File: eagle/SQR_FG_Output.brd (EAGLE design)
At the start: 42.9 x 30.5 mm, 17 parts, among them IC2 NJM7032, T1 2SK4017, T2 2SK4017

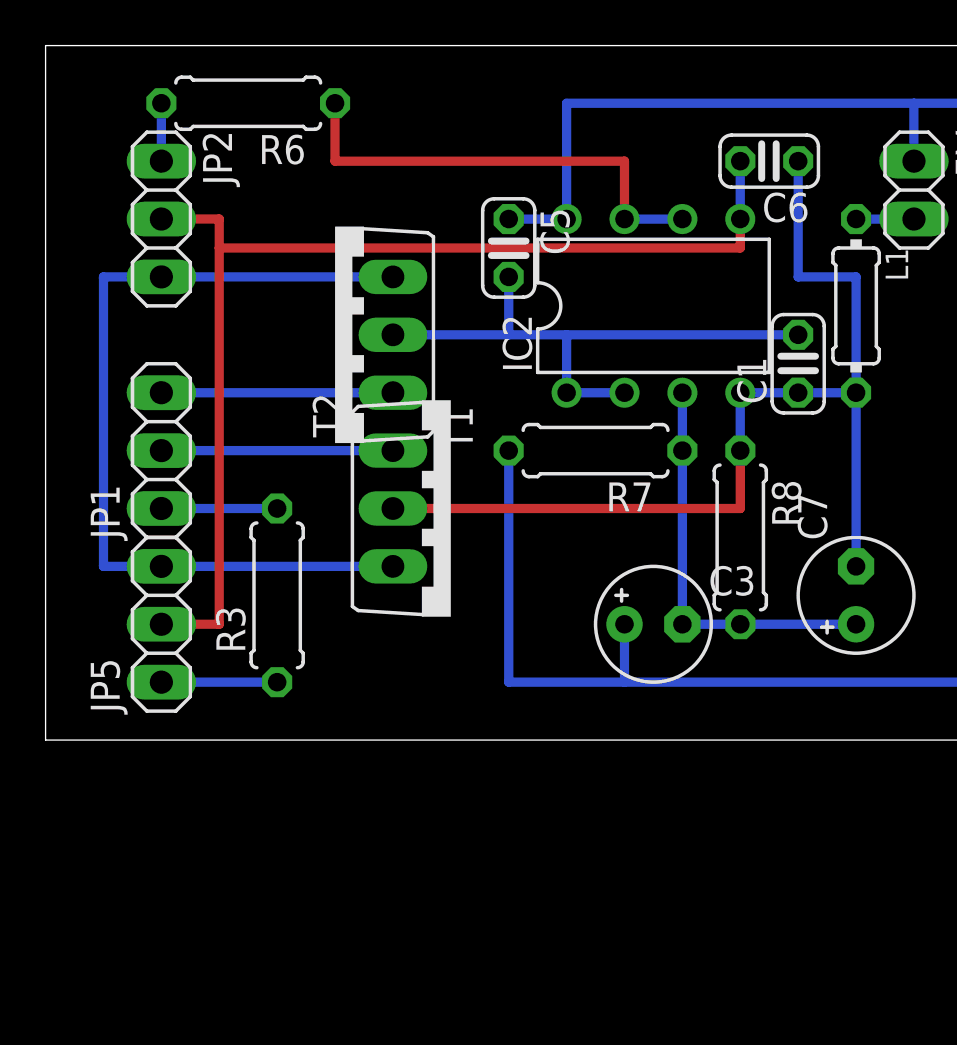
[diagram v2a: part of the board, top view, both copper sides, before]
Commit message: SQR_FG_Output.sch LC 2次LPFを追加
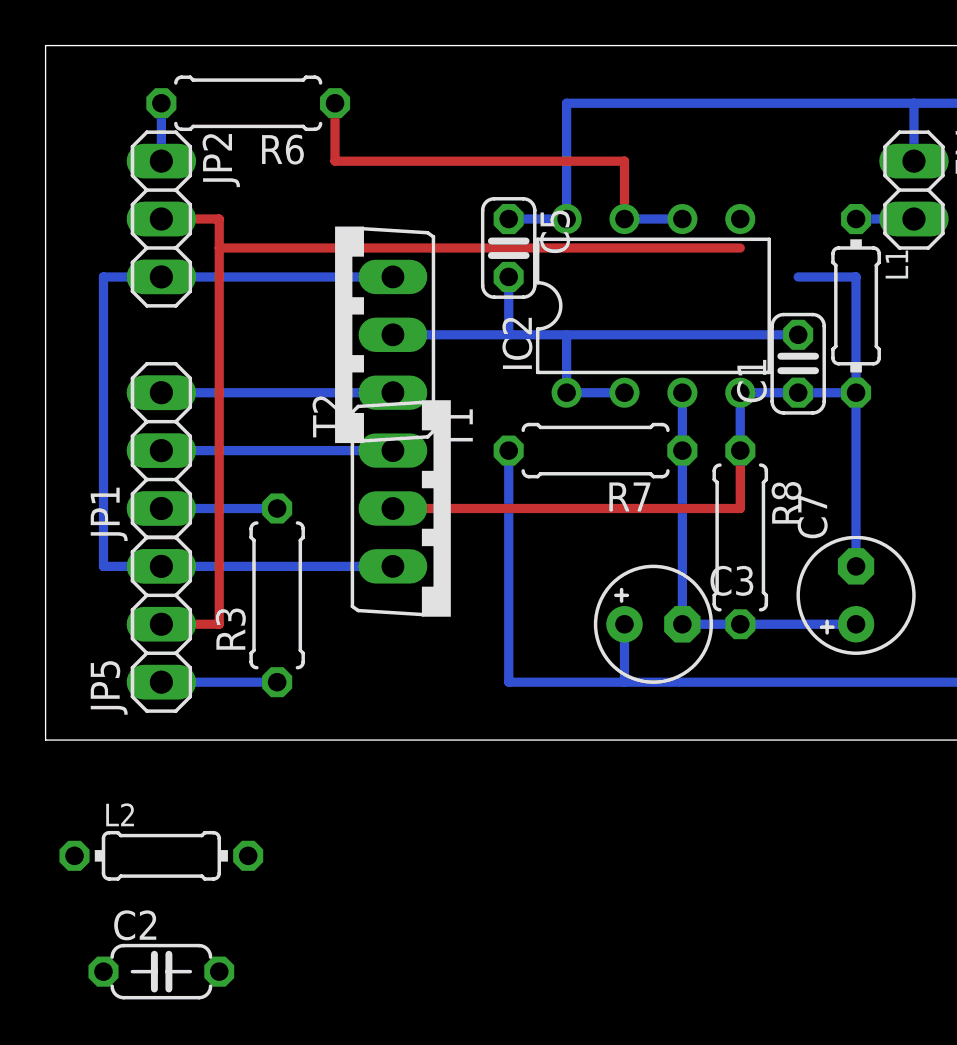
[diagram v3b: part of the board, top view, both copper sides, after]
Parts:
- removed C6: 22pF, rcl:C025-024X044
- added C2: 100p, rcl:C050-024X044
- added L2: 1uH, rcl:0204/7
- R3: value 10k -> 1k
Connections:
- new net N$1: C2.1, IC2.5, L2.2
- net AGND: no longer C6.1
- net BYPASS: now also C2.2, L2.1; no longer C6.2, IC2.5
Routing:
- net AGND: track 45.7 -> 40.6 mm
- net BYPASS: track 49.5 -> 45.7 mm
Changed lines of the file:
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@@
 <element name="C3" library="rcl" package="E2,5-5" value="100uF" x="26.67" y="5.08"/>
 <element name="C5" library="rcl" package="C025-024X044" value="0.1uF" x="20.32" y="21.59" rot="R270"/>
-<element name="C6" library="rcl" package="C025-024X044" value="22pF" x="31.75" y="25.4" rot="R180"/>
 <element name="C7" library="rcl" package="E2,5-5" value="100uF" x="35.56" y="6.35" rot="R90"/>
 <element name="IC2" library="linear" package="DIL08" value="NJM7032" x="26.67" y="19.05"/>
 <element name="JP5" library="pinhead" package="1X03" value="Level" x="5.08" y="5.08" rot="R90"/>
-<element name="R3" library="rcl" package="0207/7" value="10k" x="10.16" y="6.35" rot="R90"/>
+<element name="R3" library="rcl" package="0207/7" value="1k" x="10.16" y="6.35" rot="R90"/>
 <element name="R6" library="rcl" package="0207/7" value="10" x="8.89" y="27.94" rot="R180"/>
 <element name="R7" library="rcl" package="0207/7" value="10k" x="24.13" y="12.7" rot="R180"/>
@@
 <element name="L1" library="rcl" package="0204/7" value="1uH" x="35.56" y="19.05" rot="R270"/>
 <element name="JP2" library="pinhead" package="1X03" value="" x="5.08" y="22.86" rot="R270"/>
+<element name="L2" library="rcl" package="0204/7" value="1uH" x="5.08" y="-5.08"/>
+<element name="C2" library="rcl" package="C050-024X044" value="100p" x="5.08" y="-10.16"/>
 </elements>
 <signals>
@@
 </signal>
 <signal name="BYPASS">
-<contactref element="C6" pad="2"/>
 <contactref element="JP5" pad="2"/>
-<contactref element="IC2" pad="5"/>
-<wire x1="30.48" y1="25.4" x2="30.48" y2="22.86" width="0.4064" layer="16"/>
-<wire x1="30.48" y1="22.86" x2="30.48" y2="21.59" width="0.4064" layer="1"/>
 <wire x1="30.48" y1="21.59" x2="7.62" y2="21.59" width="0.4064" layer="1"/>
 <wire x1="7.62" y1="21.59" x2="7.62" y2="5.08" width="0.4064" layer="1"/>
@@
 <wire x1="5.08" y1="22.86" x2="7.62" y2="22.86" width="0.4064" layer="1"/>
 <wire x1="7.62" y1="22.86" x2="7.62" y2="21.59" width="0.4064" layer="1"/>
+<contactref element="L2" pad="1"/>
+<contactref element="C2" pad="2"/>
+<wire x1="1.27" y1="-5.08" x2="5.08" y2="5.08" width="0" layer="19" extent="1-1"/>
+<wire x1="7.62" y1="-10.16" x2="1.27" y2="-5.08" width="0" layer="19" extent="1-1"/>
 </signal>
 <signal name="AGND">
 <contactref element="T2" pad="2"/>
-<contactref element="C6" pad="1"/>
 <contactref element="R8" pad="1"/>
 <contactref element="C7" pad="-"/>
@@
 <wire x1="35.56" y1="15.24" x2="35.56" y2="20.32" width="0.4064" layer="16"/>
 <wire x1="35.56" y1="20.32" x2="33.02" y2="20.32" width="0.4064" layer="16"/>
-<wire x1="33.02" y1="20.32" x2="33.02" y2="25.4" width="0.4064" layer="16"/>
 <wire x1="35.56" y1="7.62" x2="35.56" y2="15.24" width="0.4064" layer="16"/>
 <wire x1="15.24" y1="10.16" x2="30.48" y2="10.16" width="0.4064" layer="1"/>
@@
 <wire x1="35.56" y1="22.86" x2="38.1" y2="22.86" width="0.4064" layer="16"/>
 </signal>
+<signal name="N$1">
+<contactref element="L2" pad="2"/>
+<contactref element="IC2" pad="5"/>
+<contactref element="C2" pad="1"/>
+<wire x1="8.89" y1="-5.08" x2="30.48" y2="22.86" width="0" layer="19" extent="1-1"/>
+<wire x1="2.54" y1="-10.16" x2="8.89" y2="-5.08" width="0" layer="19" extent="1-1"/>
+</signal>
 </signals>

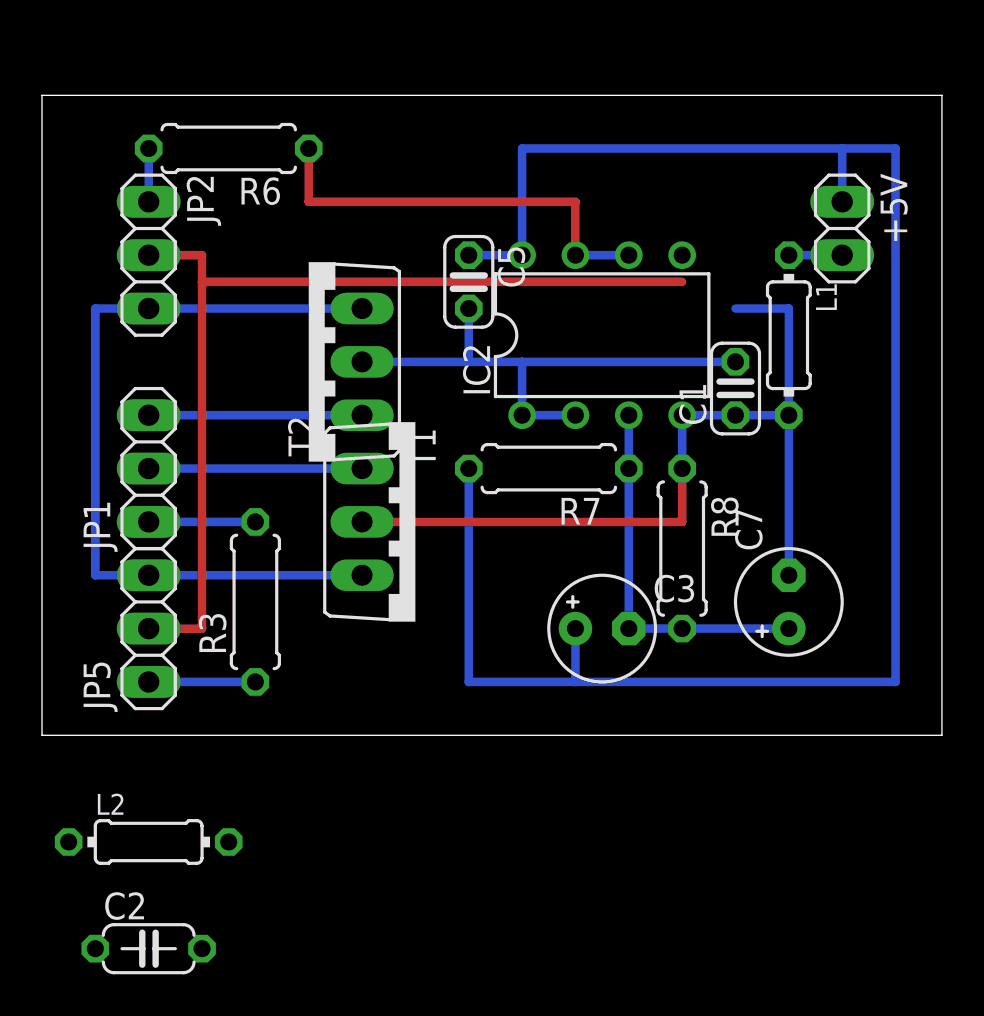
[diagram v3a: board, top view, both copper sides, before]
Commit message: SQR_FG_Output.sch, brd: MOS-FETのGate, Drain, Sourceの並びを修正
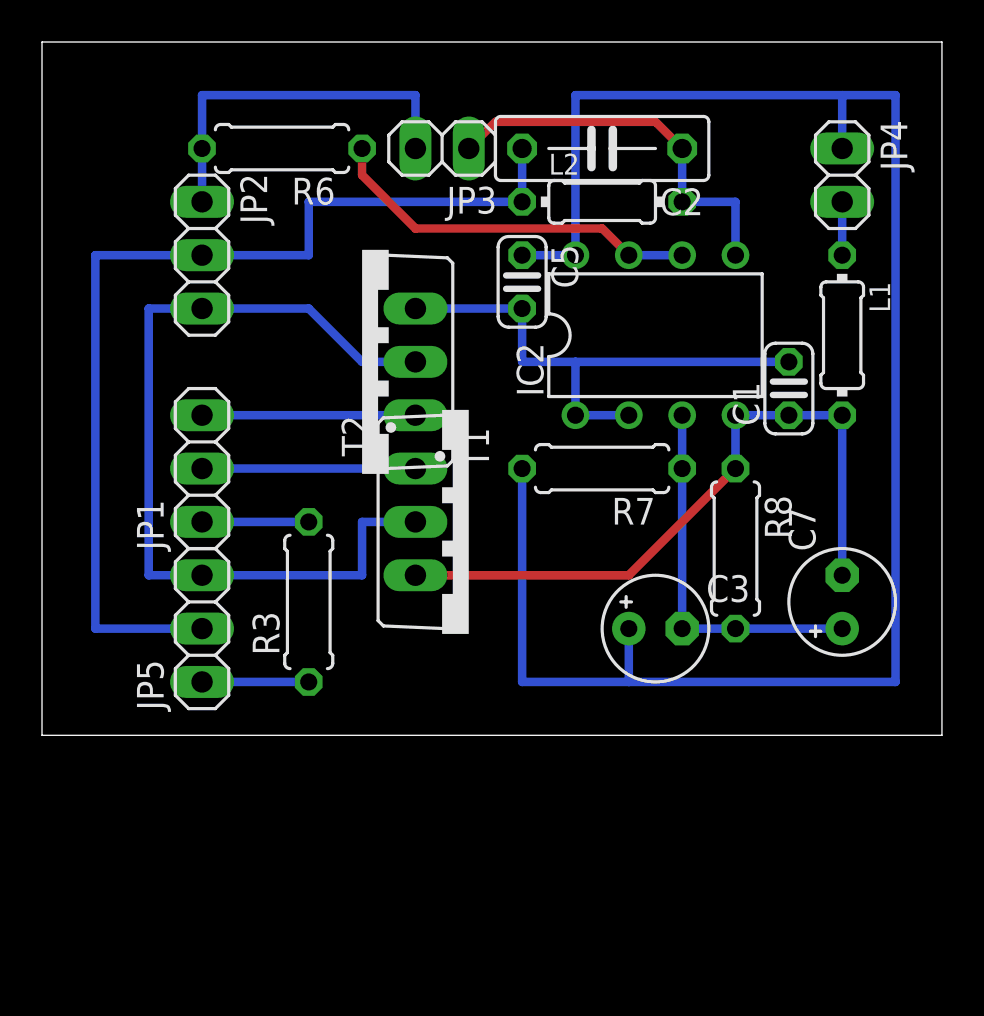
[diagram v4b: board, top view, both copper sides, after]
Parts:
- removed +5V: (no value), pinhead:1X02
- added JP3: BYPASS_BUFFER, pinhead:1X02
- added JP4: 5VIN, pinhead:1X02
- C2: device rcl:C050-024X044 -> rcl:C075-032X103
- IC2: value NJM7032 -> NJU7032
- JP2: value (none) -> OUT
- R6: value 10 -> 47
- T1, T2: device transistor-power:RD06HVF1 -> transistor-power:TO220BV
- moved C2 43.8 mm to (26.7, 27.9), turned to 180 degrees
- moved L2 37.4 mm to (26.7, 25.4)
- moved R7 2.54 mm to (26.7, 12.7)
- moved R8 2.54 mm to (33.0, 8.89)
- moved T1 2.54 mm to (15.2, 17.8)
- moved JP1 2.54 mm to (7.62, 12.7)
- moved JP2 2.54 mm to (7.62, 22.9)
- moved JP5 2.54 mm to (7.62, 5.08)
- moved C1 2.54 mm to (35.6, 16.5)
- moved C3 2.54 mm to (29.2, 5.08)
- moved C5 2.54 mm to (22.9, 21.6)
- moved C7 2.54 mm to (38.1, 6.35)
- moved IC2 2.54 mm to (29.2, 19.1)
- moved L1 2.54 mm to (38.1, 19.1)
- moved R3 2.54 mm to (12.7, 6.35)
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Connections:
- net +5V: now also JP4.1; no longer +5V.1
- net AGND: now also T2.S; no longer T2.2
- net BUFFERD: now also JP3.2
- net GND: now also JP4.2; no longer +5V.2
- net GND_OUT: now also T1.D, T2.D; no longer T1.3, T2.3
- net N$1: now also JP3.1
- net SW_GND: now also T2.G; no longer T2.1
- net SW_VGND: now also T1.G; no longer T1.1
- net VGND: now also T1.S; no longer T1.2
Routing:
- net N$1: track 0.00 -> 18.8 mm
- net BUFFERD: track 2.54 -> 17.8 mm
- net AGND: track 40.6 -> 32.6 mm
- net GND_OUT: track 38.1 -> 41.7 mm
- net BYPASS: track 45.7 -> 48.3 mm
- net N$16: track 20.3 -> 18.1 mm
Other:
- board size 42.9 x 30.5 mm -> 42.9 x 33 mm
